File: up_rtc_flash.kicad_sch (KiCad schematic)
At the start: 13 parts, among them IC201 STK8321, IC202 PCF8563T_5,518, IC203 W25Q128JVSIQTR, X201 PCIE-52P40H, X202 32.768 kHz, X203 TF-15×15

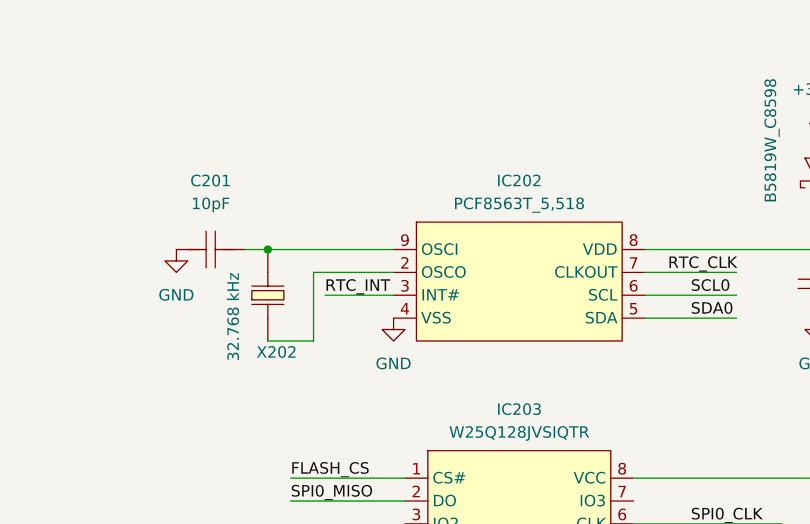
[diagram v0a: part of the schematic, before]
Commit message: fixed RTC Symbol
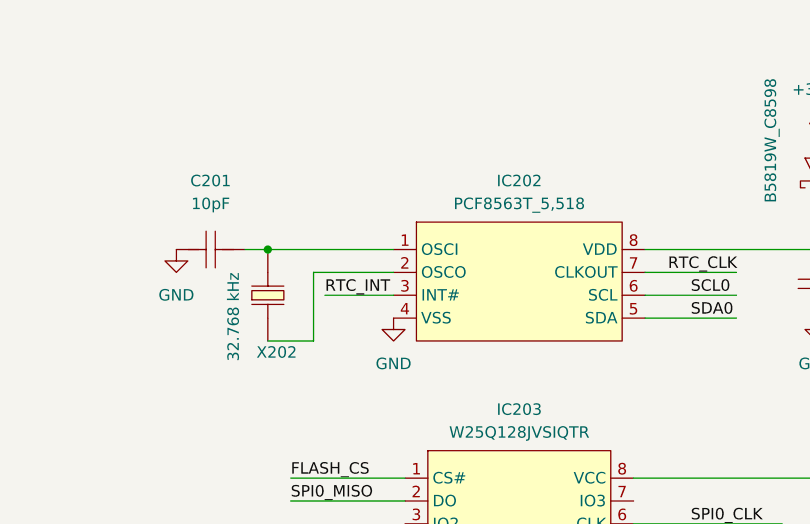
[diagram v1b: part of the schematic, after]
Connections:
- net at C201.1, X202.2: now also IC202.1 (OSCI); no longer IC202.9 (OSCI)
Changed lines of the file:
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@@
       (effects (font (size 1.27 1.27)) hide)
     )
+    (pin "1")
     (pin "2")
     (pin "3")
@@
     (pin "7")
     (pin "8")
-    (pin "9")
   )
   (symbol (lib_id "eduboardv2:GND") (at 195.58 130.81 0) (unit 1)

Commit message: changed pin types and fixed 3D-positions
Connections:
- removed net +3.3V: C202.2, C204.2, D201.2 (+), IC203.8 (VCC), X203.4 (VDD)
- removed net GND: B201.2, C201.2, C202.1, C203.1, C204.1, IC202.4 (VSS), IC203.4 (GND), X203.6 (VSS)
- new net: C204.2, IC203.8 (VCC)
- new net: C202.2, X203.4 (VDD)
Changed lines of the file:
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@@
     (pin "9")
   )
-  (symbol (lib_id "eduboardv2:B5819W_C8598") (at 247.65 39.37 0) (unit 1)
+  (symbol (lib_name "B5819W_C8598_1") (lib_id "eduboardv2:B5819W_C8598") (at 247.65 39.37 0) (unit 1)
     (in_bom yes) (on_board yes) (fields_autoplaced)
     (property "Reference" "D202" (id 0) (at 247.269 33.02 0))
@@
     (pin "2")
   )
-  (symbol (lib_id "eduboardv2:GND") (at 220.98 133.35 270) (unit 1)
+  (symbol (lib_name "GND_6") (lib_id "eduboardv2:GND") (at 220.98 133.35 270) (unit 1)
     (in_bom yes) (on_board yes)
     (property "Reference" "#PWR0206" (id 0) (at 214.63 133.35 0)
@@
     (pin "8")
   )
-  (symbol (lib_id "eduboardv2:GND") (at 190.5 72.39 0) (unit 1)
+  (symbol (lib_name "GND_2") (lib_id "eduboardv2:GND") (at 190.5 72.39 0) (unit 1)
     (in_bom yes) (on_board yes) (fields_autoplaced)
     (property "Reference" "#PWR0203" (id 0) (at 190.5 78.74 0)
@@
     (pin "2")
   )
-  (symbol (lib_id "eduboardv2:GND") (at 189.23 46.99 0) (unit 1)
+  (symbol (lib_name "GND_3") (lib_id "eduboardv2:GND") (at 189.23 46.99 0) (unit 1)
     (in_bom yes) (on_board yes) (fields_autoplaced)
     (property "Reference" "#PWR0202" (id 0) (at 189.23 53.34 0)
@@
     (pin "2")
   )
-  (symbol (lib_id "eduboardv2:+3.3V") (at 240.03 64.77 0) (unit 1)
+  (symbol (lib_name "+3.3V_1") (lib_id "eduboardv2:+3.3V") (at 240.03 64.77 0) (unit 1)
     (in_bom yes) (on_board yes) (fields_autoplaced)
     (property "Reference" "#PWR0209" (id 0) (at 240.03 68.58 0)
@@
     (pin "1")
   )
-  (symbol (lib_id "eduboardv2:GND") (at 165.1 39.37 0) (unit 1)
+  (symbol (lib_name "GND_1") (lib_id "eduboardv2:GND") (at 165.1 39.37 0) (unit 1)
     (in_bom yes) (on_board yes) (fields_autoplaced)
     (property "Reference" "#PWR0201" (id 0) (at 165.1 45.72 0)
@@
     (pin "9")
   )
-  (symbol (lib_id "eduboardv2:+3.3V") (at 236.22 26.67 0) (unit 1)
+  (symbol (lib_name "+3.3V_2") (lib_id "eduboardv2:+3.3V") (at 236.22 26.67 0) (unit 1)
     (in_bom yes) (on_board yes) (fields_autoplaced)
     (property "Reference" "#PWR0207" (id 0) (at 236.22 30.48 0)
@@
     (pin "1")
   )
-  (symbol (lib_id "eduboardv2:GND") (at 240.03 72.39 0) (unit 1)
+  (symbol (lib_name "GND_5") (lib_id "eduboardv2:GND") (at 240.03 72.39 0) (unit 1)
     (in_bom yes) (on_board yes) (fields_autoplaced)
     (property "Reference" "#PWR0210" (id 0) (at 240.03 78.74 0)
@@
     (pin "2")
   )
-  (symbol (lib_id "eduboardv2:GND") (at 252.73 52.07 0) (unit 1)
+  (symbol (lib_name "GND_7") (lib_id "eduboardv2:GND") (at 252.73 52.07 0) (unit 1)
     (in_bom yes) (on_board yes) (fields_autoplaced)
     (property "Reference" "#PWR0211" (id 0) (at 252.73 58.42 0)
@@
     (pin "1")
   )
-  (symbol (lib_id "eduboardv2:GND") (at 236.22 46.99 0) (unit 1)
+  (symbol (lib_name "GND_4") (lib_id "eduboardv2:GND") (at 236.22 46.99 0) (unit 1)
     (in_bom yes) (on_board yes) (fields_autoplaced)
     (property "Reference" "#PWR0208" (id 0) (at 236.22 53.34 0)

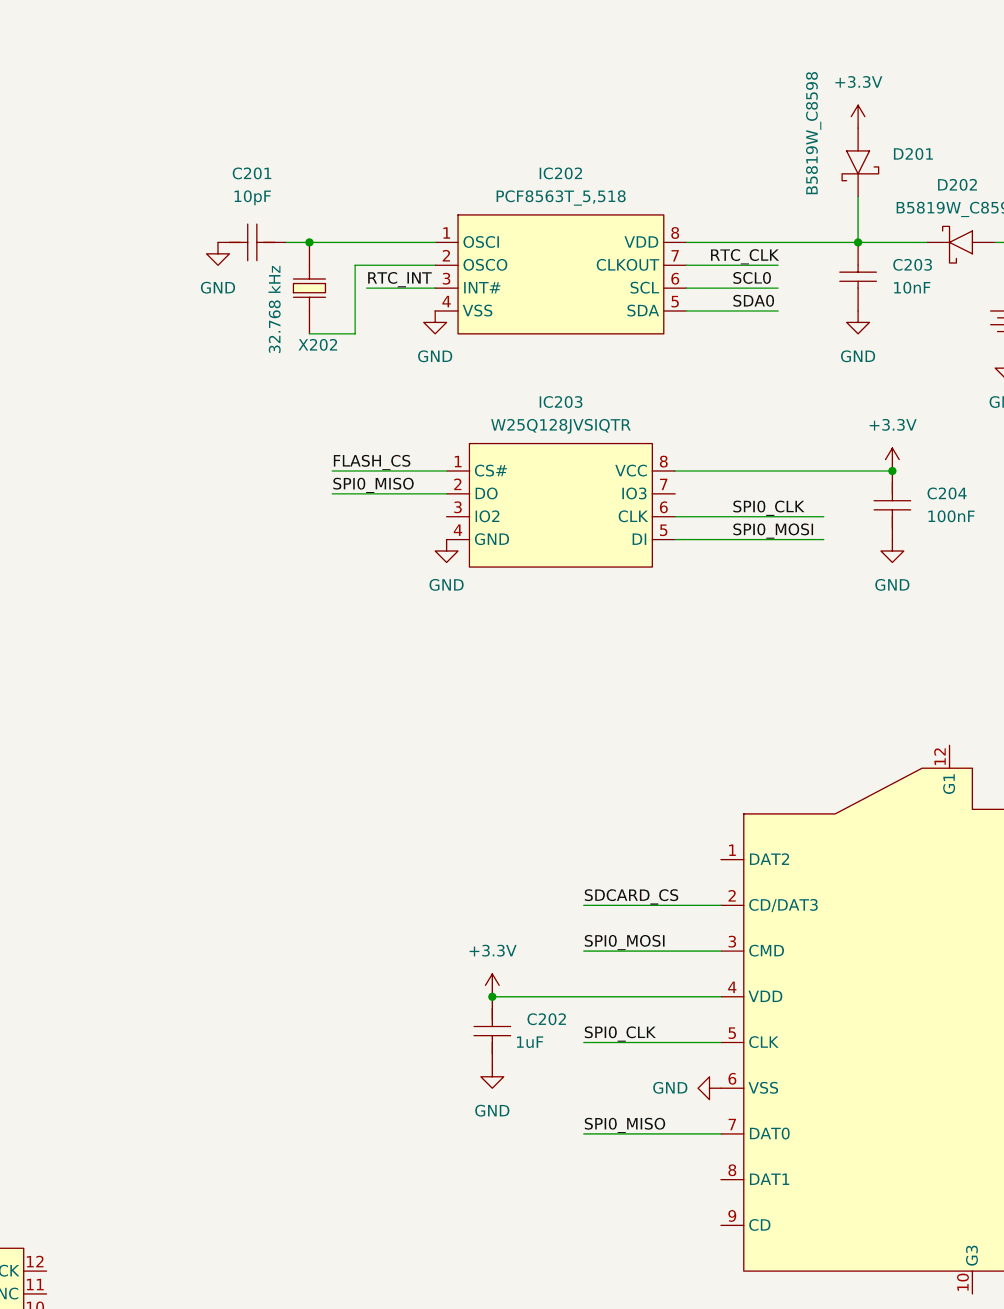
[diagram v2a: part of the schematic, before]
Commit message: change all local labels to global labels.
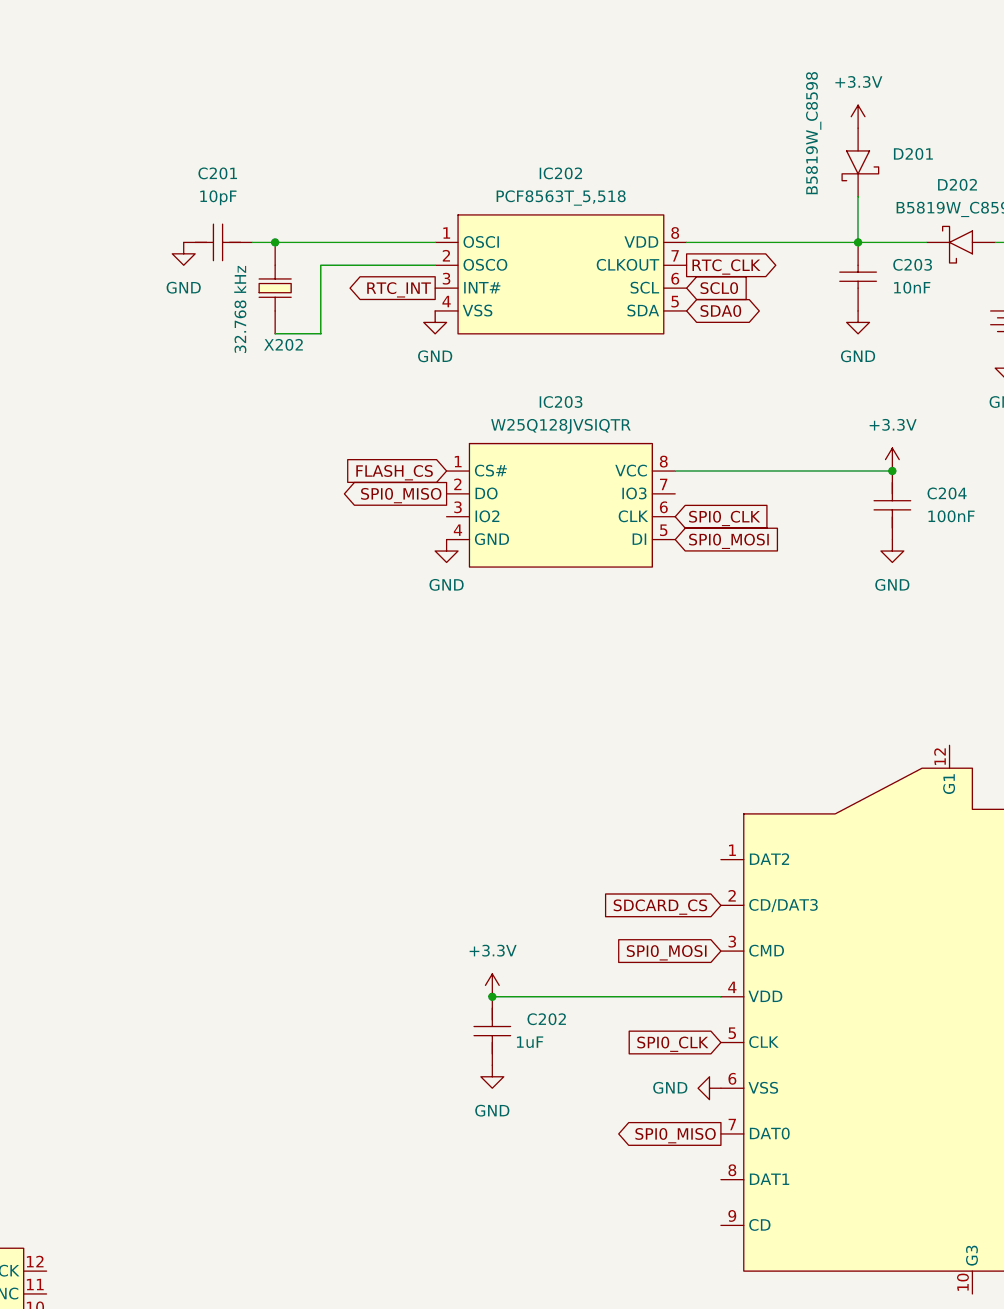
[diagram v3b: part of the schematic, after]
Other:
- moved on the sheet: C201, X202

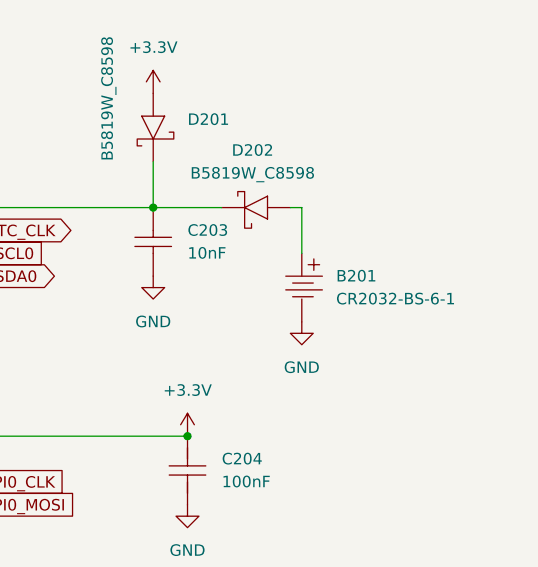
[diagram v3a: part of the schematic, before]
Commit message: positioned components. Exchanged battery holder
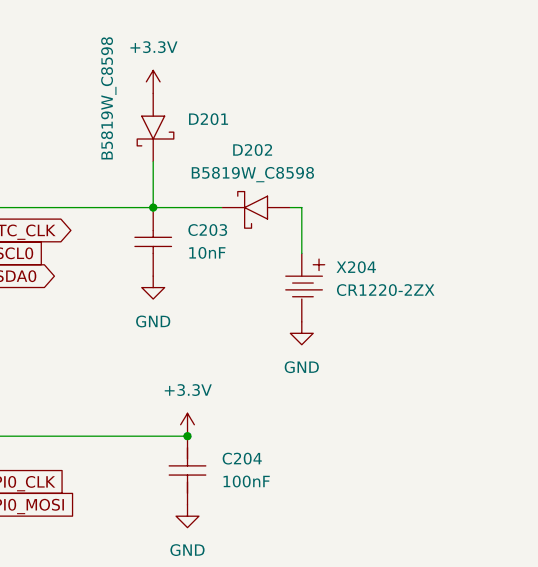
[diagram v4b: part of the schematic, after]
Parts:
- removed B201: CR2032-BS-6-1, BAT-TH_CR2032-BS-6-1, symbol eduboardv2:CR2032-BS-6-1
- added X204: CR1220-2ZX, BAT-SMD_CR1220-2ZX, symbol eduboardv2:CR1220-2ZX
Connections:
- net at D202.2 (+): now also X204.1
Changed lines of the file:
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@@
-    (pin "2")
-  )
-  (symbol (lib_id "eduboardv2:CR2032-BS-6-1") (at 252.73 48.26 270) (unit 1)
-    (in_bom yes) (on_board yes) (fields_autoplaced)
-    (property "Reference" "B201" (id 0) (at 256.54 46.9899 90)
-      (effects (font (size 1.27 1.27)) (justify left))
-    )
-    (property "Value" "CR2032-BS-6-1" (id 1) (at 256.54 49.5299 90)
-      (effects (font (size 1.27 1.27)) (justify left))
-    )
-    (property "Footprint" "BAT-TH_CR2032-BS-6-1" (id 2) (at 245.11 48.26 0)
-      (effects (font (size 1.27 1.27)) hide)
-    )
-    (property "Datasheet" "https://lcsc.com/product-detail/Battery-Holders-Clips-Contacts_Button-battery-holder-CR2032_C70377.html" (id 3) (at 240.03 48.26 0)
-      (effects (font (size 1.27 1.27)) hide)
-    )
-    (property "Manufacturer" "Q&J" (id 4) (at 237.49 48.26 0)
-      (effects (font (size 1.27 1.27)) hide)
-    )
-    (property "LCSC Part" "C70377" (id 5) (at 234.95 48.26 0)
-      (effects (font (size 1.27 1.27)) hide)
-    )
-    (property "JLC Part" "Extended Part" (id 6) (at 232.41 48.26 0)
-      (effects (font (size 1.27 1.27)) hide)
-    )
-    (property "MPN" "CR2032-BS-6-1" (id 7) (at 247.65 48.26 0)
-      (effects (font (size 1.27 1.27)) hide)
-    )
-    (pin "1")
     (pin "2")
   )
@@
       (effects (font (size 1.27 1.27)) hide)
     )
+    (pin "1")
+    (pin "2")
+  )
+  (symbol (lib_id "eduboardv2:CR1220-2ZX") (at 252.73 48.26 270) (unit 1)
+    (in_bom yes) (on_board yes) (fields_autoplaced)
+    (property "Reference" "X204" (id 0) (at 256.54 46.0405 90)
+      (effects (font (size 1.27 1.27)) (justify left))
+    )
+    (property "Value" "CR1220-2ZX" (id 1) (at 256.54 48.5805 90)
+      (effects (font (size 1.27 1.27)) (justify left))
+    )
+    (property "Footprint" "BAT-SMD_CR1220-2ZX" (id 2) (at 245.11 48.26 0)
+      (effects (font (size 1.27 1.27)) hide)
+    )
+    (property "Datasheet" "https://lcsc.com/product-detail/Battery-Holders-Clips-Contacts_Q-J-CR1220-2ZX_C969906.html" (id 3) (at 240.03 48.26 0)
+      (effects (font (size 1.27 1.27)) hide)
+    )
+    (property "Manufacturer" "Q&J" (id 4) (at 237.49 48.26 0)
+      (effects (font (size 1.27 1.27)) hide)
+    )
+    (property "LCSC Part" "C969906" (id 5) (at 234.95 48.26 0)
+      (effects (font (size 1.27 1.27)) hide)
+    )
+    (property "JLC Part" "Extended Part" (id 6) (at 232.41 48.26 0)
+      (effects (font (size 1.27 1.27)) hide)
+    )
+    (property "MPN" "CR1220-2ZX" (id 7) (at 247.65 48.26 0)
+      (effects (font (size 1.27 1.27)) hide)
+    )

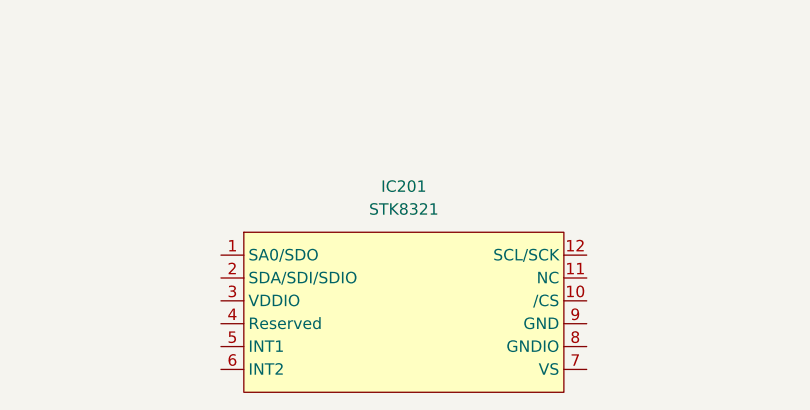
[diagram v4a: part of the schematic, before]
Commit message: move IMU to interfaces page
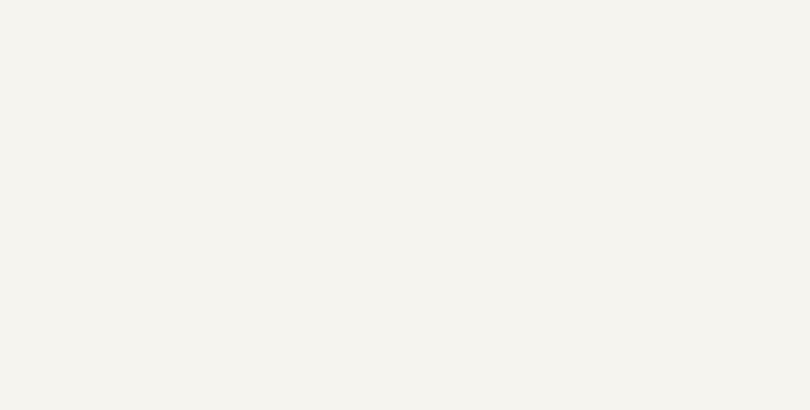
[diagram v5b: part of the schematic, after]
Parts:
- removed IC201: STK8321, LGA-12_L2.0-W2.0-P0.50-TR, symbol eduboardv2:STK8321
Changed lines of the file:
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@@
     )
-  )
-  (symbol (lib_id "eduboardv2:STK8321") (at 125.73 160.02 0) (unit 1)
-    (in_bom yes) (on_board yes) (fields_autoplaced)
-    (property "Reference" "IC201" (id 0) (at 125.73 146.05 0))
-    (property "Value" "STK8321" (id 1) (at 125.73 148.59 0))
-    (property "Footprint" "LGA-12_L2.0-W2.0-P0.50-TR" (id 2) (at 125.73 173.99 0)
-      (effects (font (size 1.27 1.27)) hide)
-    )
-    (property "Datasheet" "" (id 3) (at 125.73 160.02 0)
-      (effects (font (size 1.27 1.27)) hide)
-    )
-    (property "Manufacturer" "SENSORTEK(昇佳)" (id 4) (at 125.73 179.07 0)
-      (effects (font (size 1.27 1.27)) hide)
-    )
-    (property "LCSC Part" "C966924" (id 5) (at 125.73 181.61 0)
-      (effects (font (size 1.27 1.27)) hide)
-    )
-    (property "JLC Part" "Extended Part" (id 6) (at 125.73 184.15 0)
-      (effects (font (size 1.27 1.27)) hide)
-    )
-    (property "MPN" "STK8321" (id 7) (at 125.73 171.45 0)
-      (effects (font (size 1.27 1.27)) hide)
-    )
-    (pin "1")
-    (pin "10")
-    (pin "11")
-    (pin "12")
-    (pin "2")
-    (pin "3")
-    (pin "4")
-    (pin "5")
-    (pin "6")
-    (pin "7")
-    (pin "8")
-    (pin "9")
   )
   (symbol (lib_name "B5819W_C8598_1") (lib_id "eduboardv2:B5819W_C8598") (at 247.65 39.37 0) (unit 1)
